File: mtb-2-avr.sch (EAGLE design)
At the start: 14 parts, among them IC1 MEGA8-AI, Q1 14.745 MHz

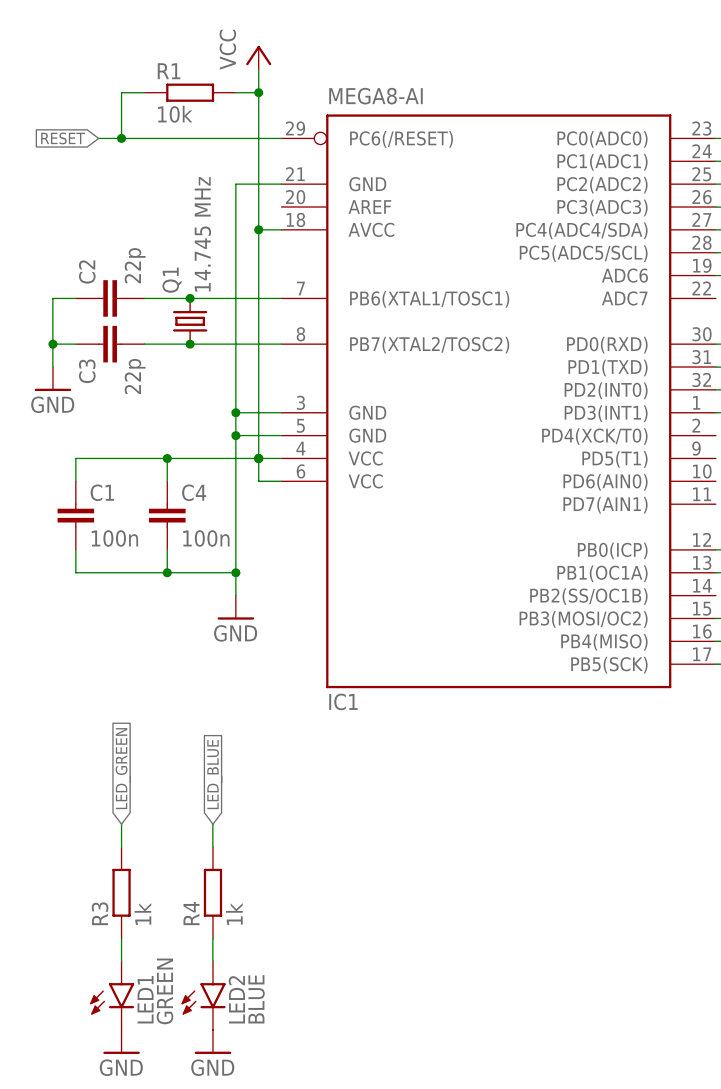
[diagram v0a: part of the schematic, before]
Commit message: Add LCSC parts numbers.
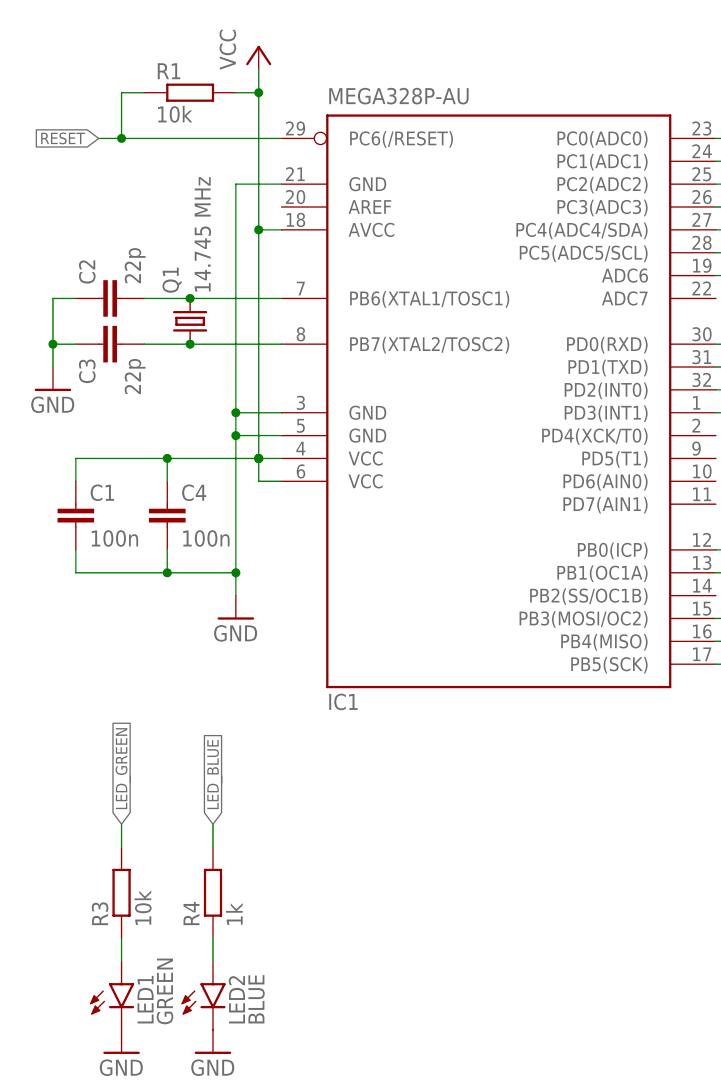
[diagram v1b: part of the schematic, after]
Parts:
- C1, C4: LCSC_PART (none) -> C14663
- C2, C3: LCSC_PART (none) -> C1653
- IC1: value MEGA8-AI -> MEGA328P-AU; LCSC_PART (none) -> C14877
- LED1: LCSC_PART (none) -> C72043
- LED2: LCSC_PART (none) -> C72041
- R1, R2: LCSC_PART (none) -> C25804
- R3: value 1k -> 10k; LCSC_PART (none) -> C25804
- R4: LCSC_PART (none) -> C21190
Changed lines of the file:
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@@
 <part name="P+1" library="supply1" library_urn="urn:adsk.eagle:library:371" deviceset="VCC" device=""/>
 <part name="GND1" library="supply1" library_urn="urn:adsk.eagle:library:371" deviceset="GND" device=""/>
-<part name="IC1" library="atmel" library_urn="urn:adsk.eagle:library:105" deviceset="MEGA8" device="-AI" package3d_urn="urn:adsk.eagle:package:4313/2"/>
-<part name="C1" library="rcl" deviceset="C-EU" device="C0603" value="100n"/>
-<part name="R1" library="rcl" deviceset="R-EU_" device="R0603" value="10k"/>
-<part name="LED1" library="led" library_urn="urn:adsk.eagle:library:259" deviceset="LED" device="CHIPLED_0603" package3d_urn="urn:adsk.eagle:package:15822/2" value="GREEN"/>
-<part name="LED2" library="led" library_urn="urn:adsk.eagle:library:259" deviceset="LED" device="CHIPLED_0603" package3d_urn="urn:adsk.eagle:package:15822/2" value="BLUE"/>
+<part name="IC1" library="atmel" library_urn="urn:adsk.eagle:library:105" deviceset="MEGA8" device="-AI" package3d_urn="urn:adsk.eagle:package:4313/2" value="MEGA328P-AU">
+<attribute name="LCSC_PART" value="C14877"/>
+</part>
+<part name="C1" library="rcl" deviceset="C-EU" device="C0603" value="100n">
+<attribute name="LCSC_PART" value="C14663"/>
+</part>
+<part name="R1" library="rcl" deviceset="R-EU_" device="R0603" value="10k">
+<attribute name="LCSC_PART" value="C25804"/>
+</part>
+<part name="LED1" library="led" library_urn="urn:adsk.eagle:library:259" deviceset="LED" device="CHIPLED_0603" package3d_urn="urn:adsk.eagle:package:15822/2" value="GREEN">
+<attribute name="LCSC_PART" value="C72043"/>
+</part>
+<part name="LED2" library="led" library_urn="urn:adsk.eagle:library:259" deviceset="LED" device="CHIPLED_0603" package3d_urn="urn:adsk.eagle:package:15822/2" value="BLUE">
+<attribute name="LCSC_PART" value="C72041"/>
+</part>
 <part name="Q1" library="crystal" library_urn="urn:adsk.eagle:library:204" deviceset="CRYSTAL" device="HC49UP" package3d_urn="urn:adsk.eagle:package:12078/1" value="14.745 MHz"/>
 <part name="GND2" library="supply1" library_urn="urn:adsk.eagle:library:371" deviceset="GND" device=""/>
-<part name="C2" library="rcl" deviceset="C-EU" device="C0603" value="22p"/>
-<part name="C3" library="rcl" deviceset="C-EU" device="C0603" value="22p"/>
+<part name="C2" library="rcl" deviceset="C-EU" device="C0603" value="22p">
+<attribute name="LCSC_PART" value="C1653"/>
+</part>
+<part name="C3" library="rcl" deviceset="C-EU" device="C0603" value="22p">
+<attribute name="LCSC_PART" value="C1653"/>
+</part>
 <part name="GND3" library="supply1" library_urn="urn:adsk.eagle:library:371" deviceset="GND" device=""/>
 <part name="P+2" library="supply1" library_urn="urn:adsk.eagle:library:371" deviceset="VCC" device=""/>
-<part name="C4" library="rcl" deviceset="C-EU" device="C0603" value="100n"/>
+<part name="C4" library="rcl" deviceset="C-EU" device="C0603" value="100n">
+<attribute name="LCSC_PART" value="C14663"/>
+</part>
 <part name="ISP1" library="adafruit" library_urn="urn:adsk.eagle:library:420" deviceset="AVRISP" device="-6" package3d_urn="urn:adsk.eagle:package:6240744/1"/>
 <part name="P+4" library="supply1" library_urn="urn:adsk.eagle:library:371" deviceset="VCC" device=""/>
 <part name="GND5" library="supply1" library_urn="urn:adsk.eagle:library:371" deviceset="GND" device=""/>
-<part name="R2" library="rcl" deviceset="R-EU_" device="R0603" value="10k"/>
+<part name="R2" library="rcl" deviceset="R-EU_" device="R0603" value="10k">
+<attribute name="LCSC_PART" value="C25804"/>
+</part>
 <part name="P+5" library="supply1" library_urn="urn:adsk.eagle:library:371" deviceset="VCC" device=""/>
 <part name="GND6" library="supply1" library_urn="urn:adsk.eagle:library:371" deviceset="GND" device=""/>
 <part name="GND7" library="supply1" library_urn="urn:adsk.eagle:library:371" deviceset="GND" device=""/>
-<part name="R3" library="rcl" deviceset="R-EU_" device="R0603" value="1k"/>
-<part name="R4" library="rcl" deviceset="R-EU_" device="R0603" value="1k"/>
+<part name="R3" library="rcl" deviceset="R-EU_" device="R0603" value="10k">
+<attribute name="LCSC_PART" value="C25804"/>
+</part>
+<part name="R4" library="rcl" deviceset="R-EU_" device="R0603" value="1k">
+<attribute name="LCSC_PART" value="C21190"/>
+</part>
 </parts>
 <sheets>
@@
 <attribute name="NAME" x="40.64" y="50.8" size="1.778" layer="95"/>
 <attribute name="VALUE" x="40.64" y="118.11" size="1.778" layer="96"/>
+<attribute name="LCSC_PART" x="58.42" y="88.9" size="1.778" layer="96" display="off"/>
 </instance>
 <instance part="C1" gate="G$1" x="12.7" y="73.66" smashed="yes">
 <attribute name="NAME" x="14.224" y="74.041" size="1.778" layer="95"/>
 <attribute name="VALUE" x="14.224" y="68.961" size="1.778" layer="96"/>
+<attribute name="LCSC_PART" x="12.7" y="73.66" size="1.778" layer="96" display="off"/>
 </instance>
 <instance part="R1" gate="G$1" x="25.4" y="119.38" smashed="yes">
 <attribute name="NAME" x="21.59" y="120.8786" size="1.778" layer="95"/>
 <attribute name="VALUE" x="21.59" y="116.078" size="1.778" layer="96"/>
+<attribute name="LCSC_PART" x="25.4" y="119.38" size="1.778" layer="96" display="off"/>
 </instance>
 <instance part="LED1" gate="G$1" x="17.78" y="20.32" smashed="yes">
 <attribute name="NAME" x="21.336" y="15.748" size="1.778" layer="95" rot="R90"/>
 <attribute name="VALUE" x="23.495" y="15.748" size="1.778" layer="96" rot="R90"/>
+<attribute name="LCSC_PART" x="17.78" y="20.32" size="1.778" layer="96" display="off"/>
 </instance>
 <instance part="LED2" gate="G$1" x="27.94" y="20.32" smashed="yes">
 <attribute name="NAME" x="31.496" y="15.748" size="1.778" layer="95" rot="R90"/>
 <attribute name="VALUE" x="33.655" y="15.748" size="1.778" layer="96" rot="R90"/>
+<attribute name="LCSC_PART" x="27.94" y="20.32" size="1.778" layer="96" display="off"/>
 </instance>
 <instance part="Q1" gate="G$1" x="25.4" y="93.98" smashed="yes" rot="R90">
@@
 <attribute name="NAME" x="14.859" y="98.044" size="1.778" layer="95" rot="R90"/>
 <attribute name="VALUE" x="19.939" y="98.044" size="1.778" layer="96" rot="R90"/>
+<attribute name="LCSC_PART" x="15.24" y="96.52" size="1.778" layer="96" rot="R90" display="off"/>
 </instance>
 <instance part="C3" gate="G$1" x="15.24" y="91.44" smashed="yes" rot="MR270">
 <attribute name="NAME" x="14.859" y="89.916" size="1.778" layer="95" rot="MR270"/>
 <attribute name="VALUE" x="19.939" y="89.916" size="1.778" layer="96" rot="MR270"/>
+<attribute name="LCSC_PART" x="15.24" y="91.44" size="1.778" layer="96" rot="MR270" display="off"/>
 </instance>
 <instance part="GND3" gate="1" x="10.16" y="86.36" smashed="yes">
@@
 <attribute name="NAME" x="24.384" y="74.041" size="1.778" layer="95"/>
 <attribute name="VALUE" x="24.384" y="68.961" size="1.778" layer="96"/>
+<attribute name="LCSC_PART" x="22.86" y="73.66" size="1.778" layer="96" display="off"/>
 </instance>
 <instance part="ISP1" gate="G$1" x="142.24" y="45.72" smashed="yes">
@@
 <attribute name="NAME" x="115.3414" y="110.49" size="1.778" layer="95" rot="R90"/>
 <attribute name="VALUE" x="120.142" y="110.49" size="1.778" layer="96" rot="R90"/>
+<attribute name="LCSC_PART" x="116.84" y="114.3" size="1.778" layer="96" rot="R90" display="off"/>
 </instance>
 <instance part="P+5" gate="VCC" x="116.84" y="121.92" smashed="yes">
@@
 <attribute name="NAME" x="16.2814" y="26.67" size="1.778" layer="95" rot="R90"/>
 <attribute name="VALUE" x="21.082" y="26.67" size="1.778" layer="96" rot="R90"/>
+<attribute name="LCSC_PART" x="17.78" y="30.48" size="1.778" layer="96" rot="R90" display="off"/>
 </instance>
 <instance part="R4" gate="G$1" x="27.94" y="30.48" smashed="yes" rot="R90">
 <attribute name="NAME" x="26.4414" y="26.67" size="1.778" layer="95" rot="R90"/>
 <attribute name="VALUE" x="31.242" y="26.67" size="1.778" layer="96" rot="R90"/>
+<attribute name="LCSC_PART" x="27.94" y="30.48" size="1.778" layer="96" rot="R90" display="off"/>
 </instance>
 </instances>

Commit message: Minor fixes.
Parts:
- Q1: LCSC_PART (none) -> C19646
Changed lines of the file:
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@@
 <attribute name="LCSC_PART" value="C72041"/>
 </part>
-<part name="Q1" library="crystal" library_urn="urn:adsk.eagle:library:204" deviceset="CRYSTAL" device="HC49UP" package3d_urn="urn:adsk.eagle:package:12078/1" value="14.745 MHz"/>
+<part name="Q1" library="crystal" library_urn="urn:adsk.eagle:library:204" deviceset="CRYSTAL" device="HC49UP" package3d_urn="urn:adsk.eagle:package:12078/1" value="14.745 MHz">
+<attribute name="LCSC_PART" value="C19646"/>
+</part>
 <part name="GND2" library="supply1" library_urn="urn:adsk.eagle:library:371" deviceset="GND" device=""/>
 <part name="C2" library="rcl" deviceset="C-EU" device="C0603" value="22p">
@@
 <attribute name="NAME" x="24.13" y="97.028" size="1.778" layer="95" rot="R90"/>
 <attribute name="VALUE" x="27.686" y="97.028" size="1.778" layer="96" rot="R90"/>
+<attribute name="LCSC_PART" x="25.4" y="93.98" size="1.778" layer="96" rot="R90" display="off"/>
 </instance>
 <instance part="GND2" gate="1" x="30.48" y="60.96" smashed="yes">

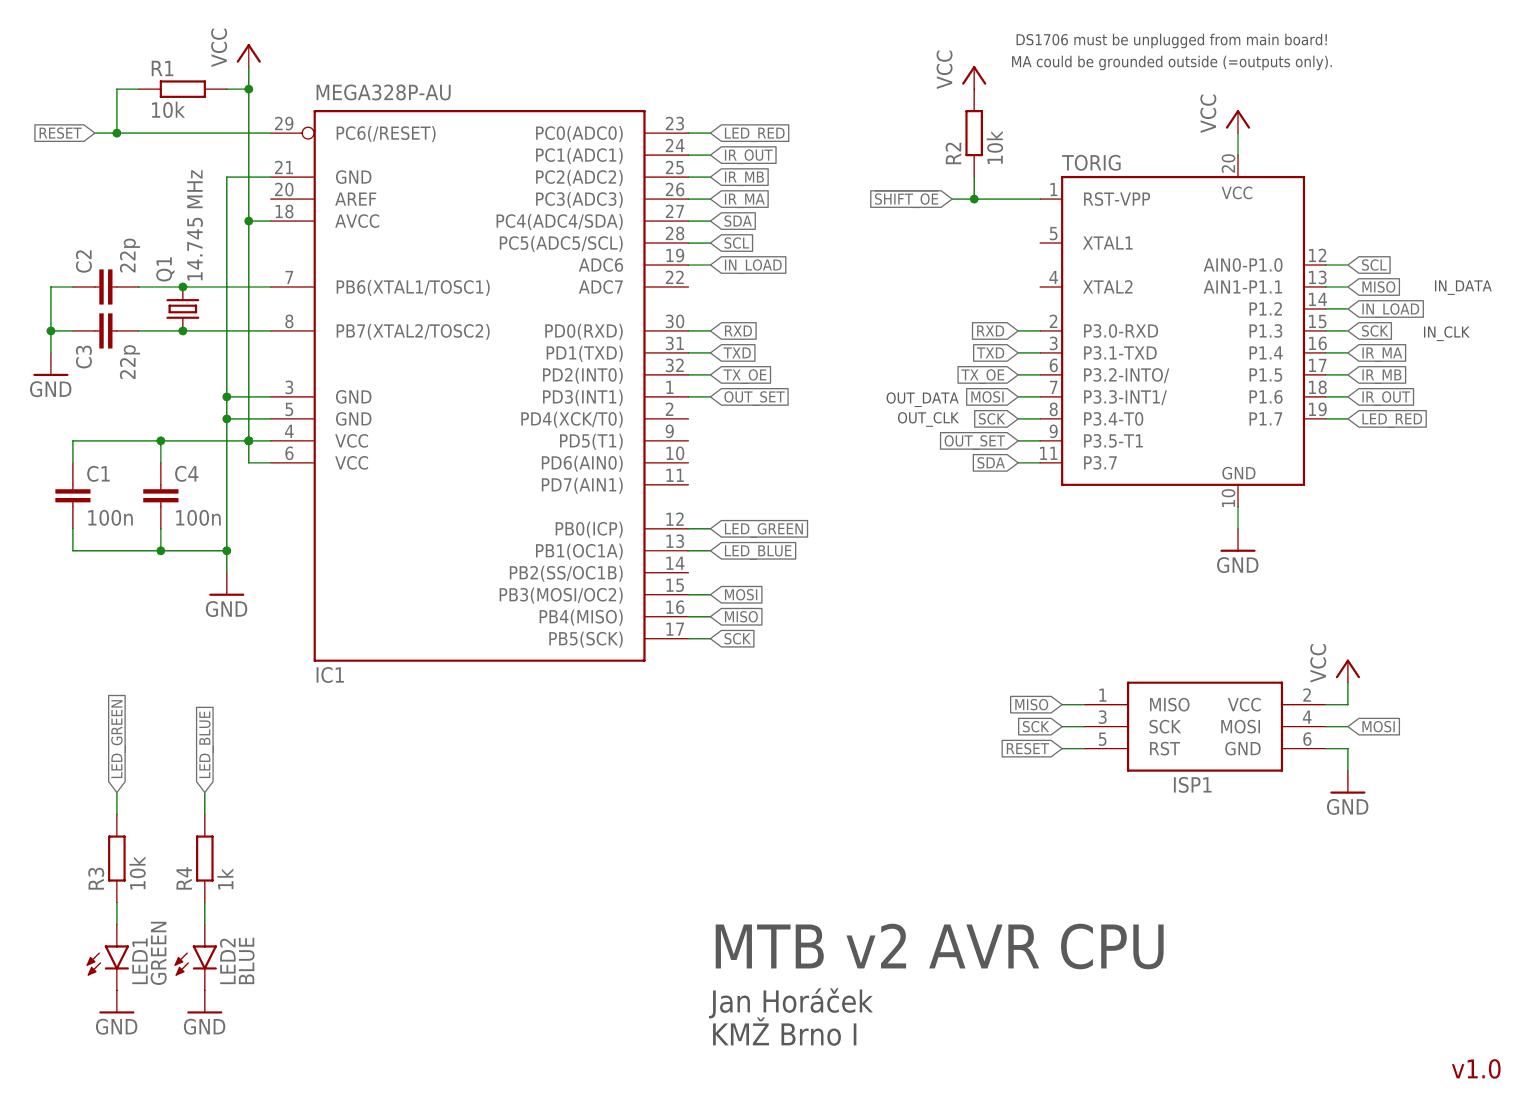
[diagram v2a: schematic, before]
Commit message: Add button, rewire, remove prog. connector.
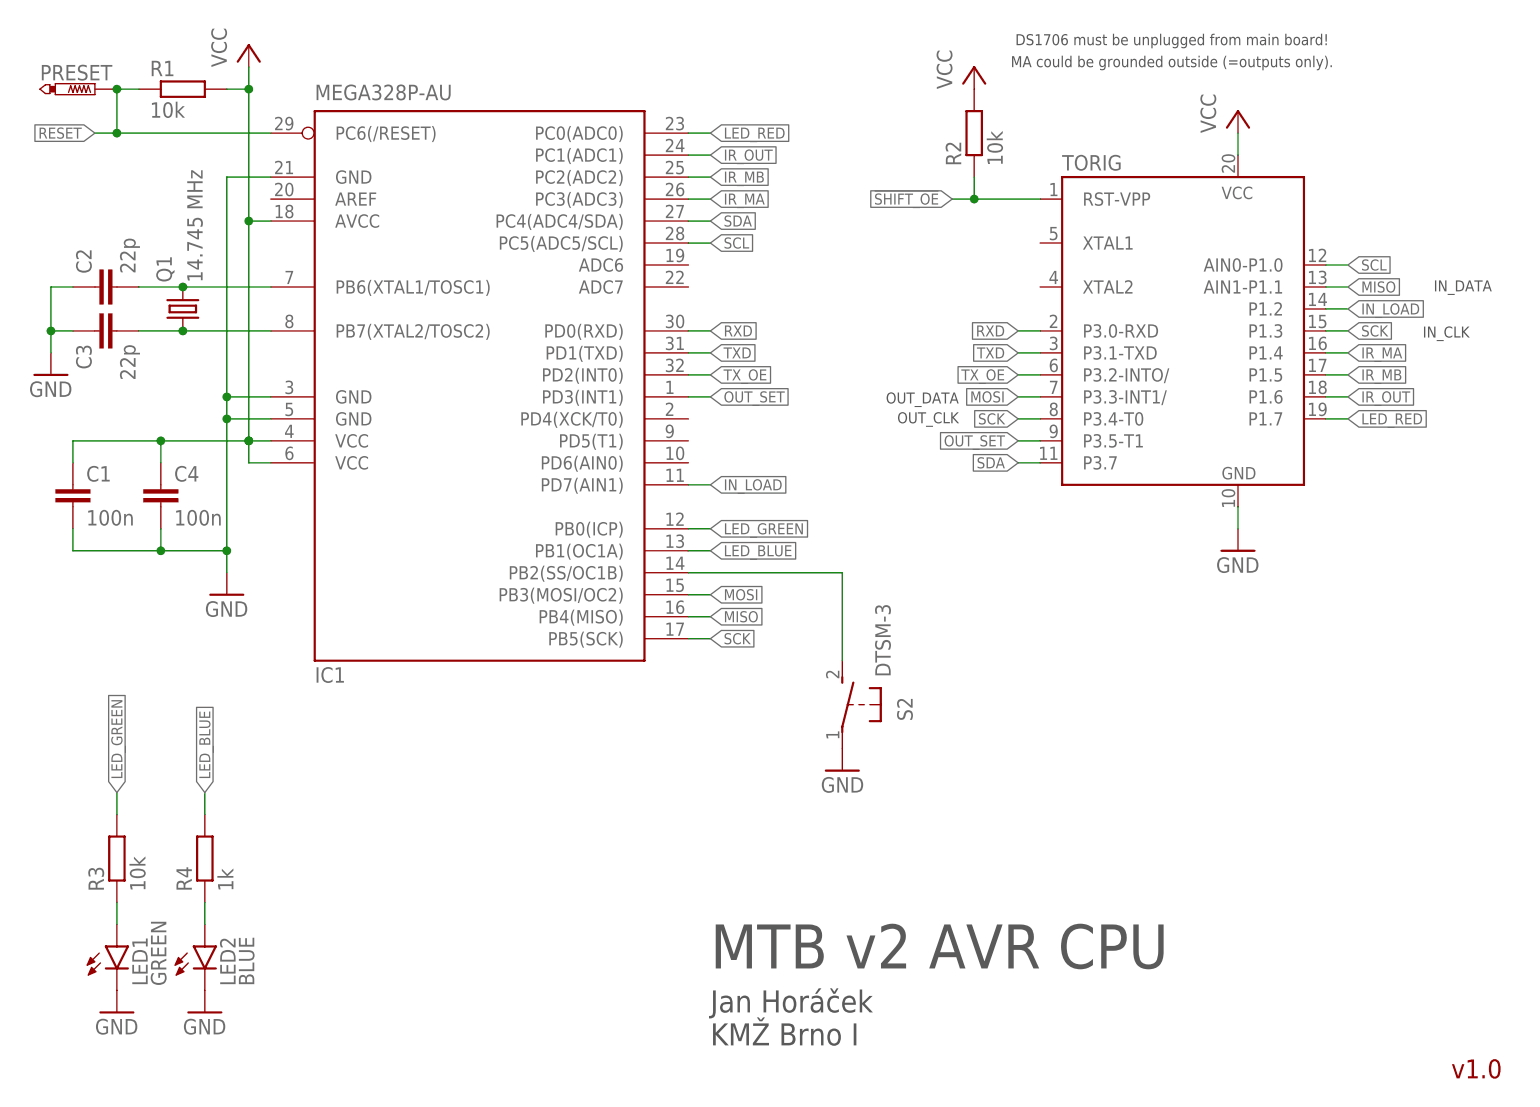
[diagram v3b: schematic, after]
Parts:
- removed ISP1: AVRISP-6, adafruit:AVRISP-6
- added PRESET: PTR1B1,27, testpad:PTR1B1,27
- added S2: DTSM-3, switch-tact:DTSM-3
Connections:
- new net N$5: IC1.PB2(SS/OC1B), S2.2
- net GND: now also S2.1; no longer ISP1.GND
- net IN_LOAD: now also IC1.PD7(AIN1); no longer IC1.ADC6
- net MISO: no longer ISP1.MISO
- net MOSI: no longer ISP1.MOSI
- net RESET: now also PRESET.TP; no longer ISP1.RST
- net SCK: no longer ISP1.SCK
- net VCC: no longer ISP1.VCC
